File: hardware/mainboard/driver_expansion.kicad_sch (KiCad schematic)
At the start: 17 parts, among them T1 V_{SA}, T10 TestPoint, T11 TestPoint, T12 TestPoint, T13 TestPoint, T14 TestPoint, T15 TestPoint, T2 Gnd, T3 Clk, T4 SClk, T5 Gnd, T6 MOSI, T7 MISO, T8 V_{CC}IO, T9 TestPoint

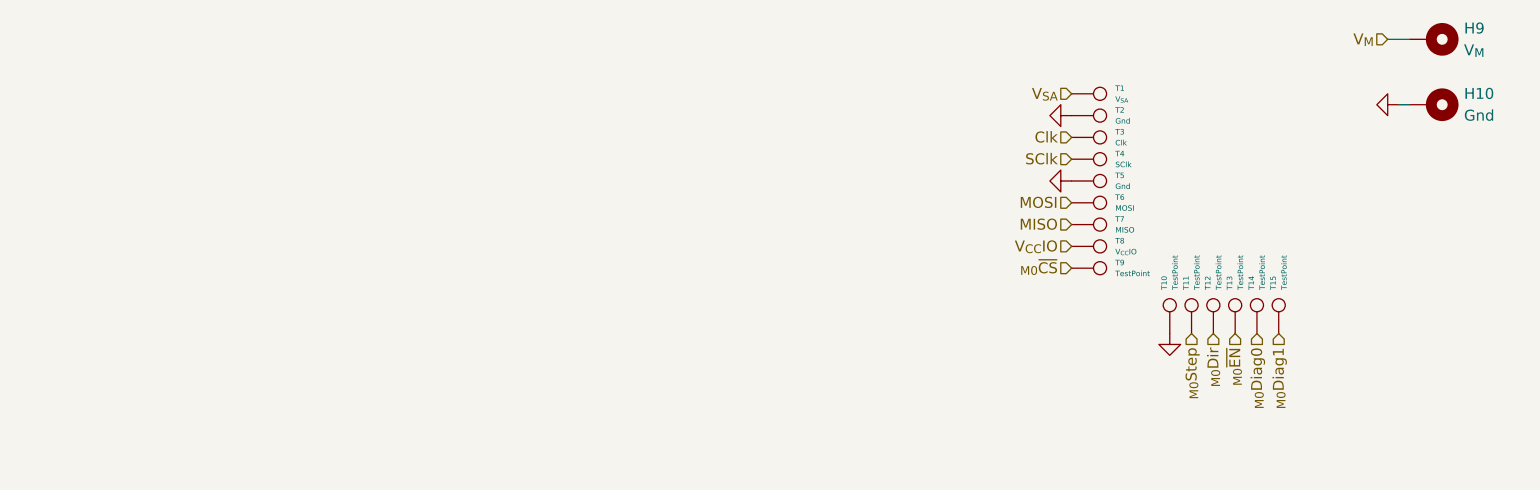
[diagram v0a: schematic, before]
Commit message: added fan / heater ports to mainboard, and footprints for switches, transistors, etc.
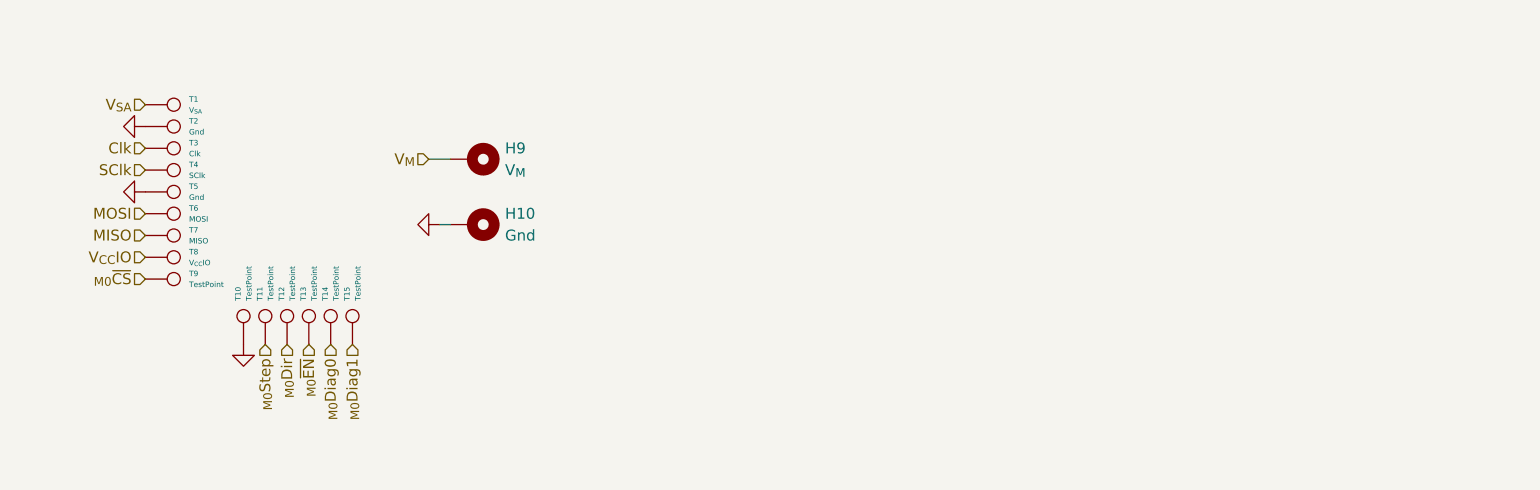
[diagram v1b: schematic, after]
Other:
- title: (none) -> Motor Expansion Socket
- moved on the sheet: H10, H9, T1, T10, T11, T12, T13, T14, T15, T2, T3, T4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

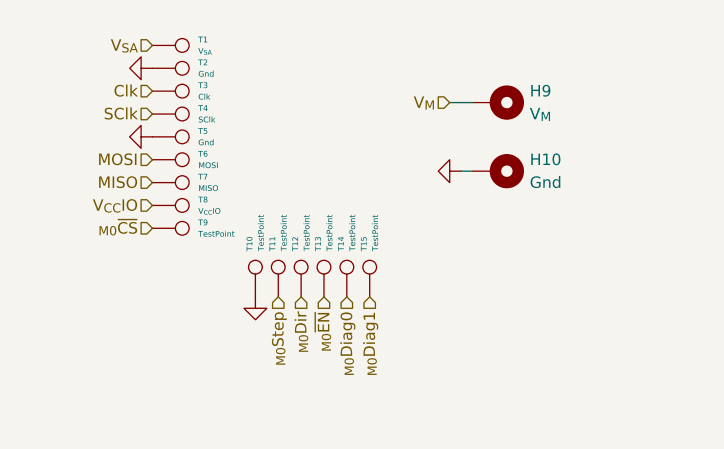
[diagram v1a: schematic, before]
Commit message: saving mainboard, gonna tear out the entire thing and redo in 4-layer
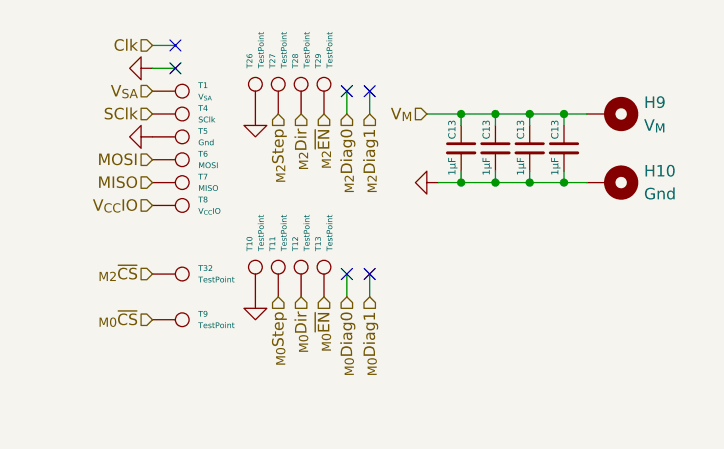
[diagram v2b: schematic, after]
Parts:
- removed T14, T15: TestPoint, corevus:LGA_Spring, symbol Connector:TestPoint
- removed T2: Gnd, corevus:LGA_Spring, symbol Connector:TestPoint
- removed T3: Clk, corevus:LGA_Spring, symbol Connector:TestPoint
- added C13 (x4): 1μF, Capacitor_SMD:C_0805_2012Metric, symbol Device:C_Small
- added T26, T27, T28, T29, T32: TestPoint, corevus:LGA_Spring, symbol Connector:TestPoint
- H10, H9: footprint corevus:M3_PCB_Nut -> corevus:M3_M2.5_PCB_Nut
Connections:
- net GND: now also C13.2, C13.2, C13.2, C13.2, T26.1
- net V_{M}: now also C13.1, C13.1, C13.1, C13.1
- new net _{M2}Dir: T28.1
- new net _{M2}Step: T27.1
- new net _{M2}~{CS}: T32.1
- new net _{M2}~{EN}: T29.1
- no-connect marks 0 -> 6
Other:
- moved on the sheet: H10, H9, T1, T9

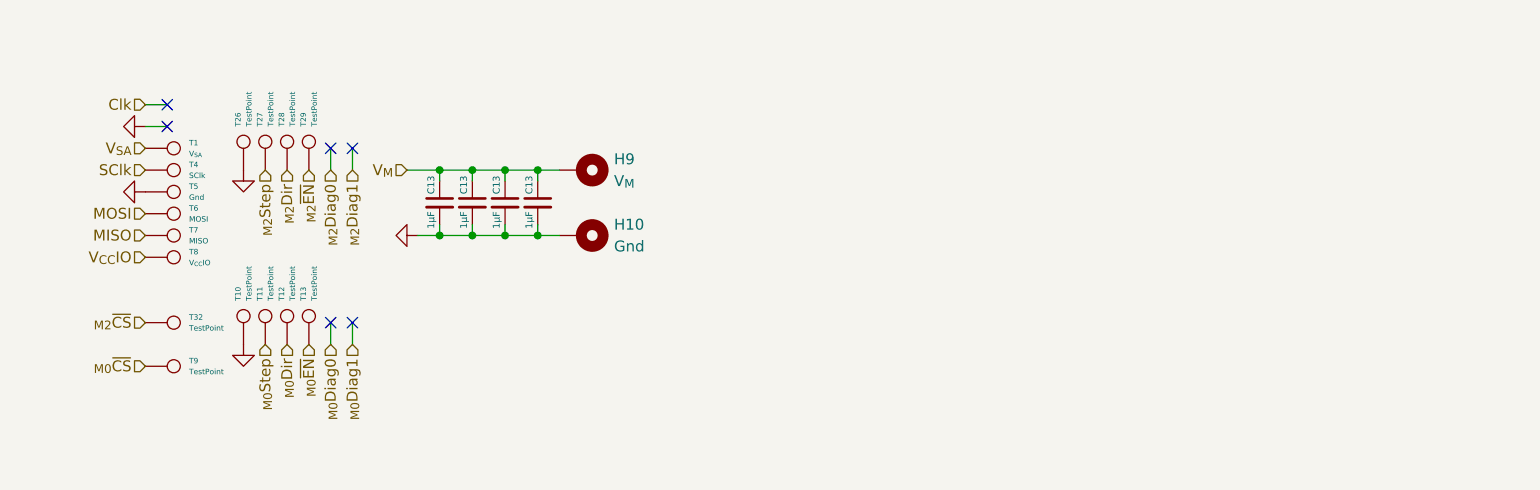
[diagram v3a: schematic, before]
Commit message: redid mainboard, added probe wiring, replacing ncp chip with LM5160 for now
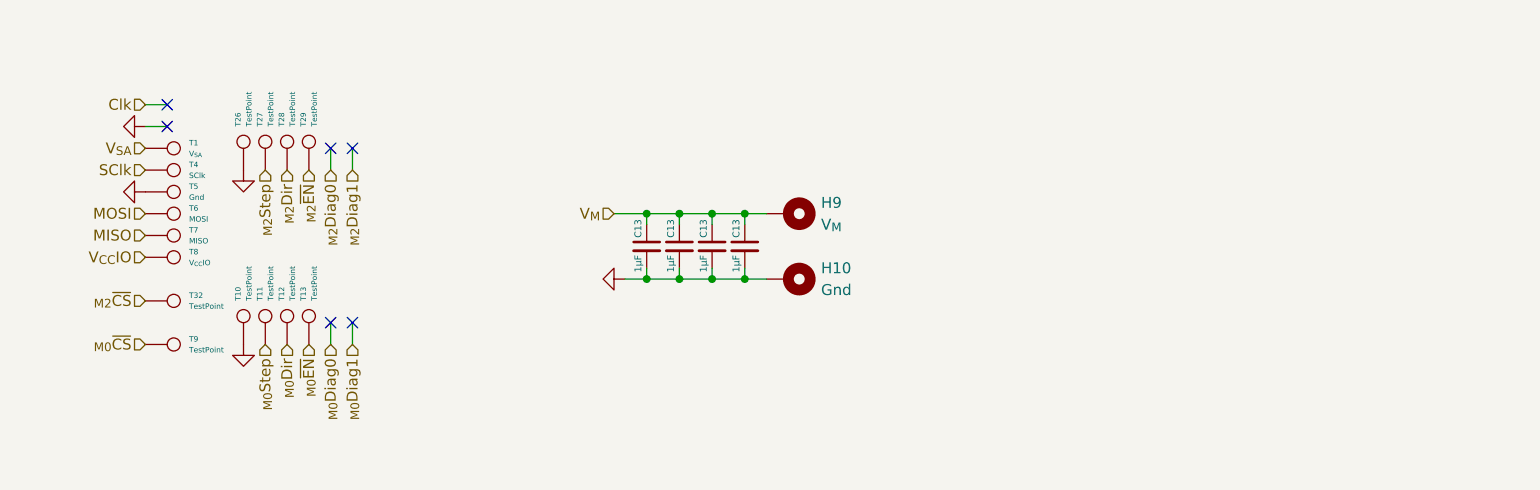
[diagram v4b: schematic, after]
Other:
- moved on the sheet: C13, H10, H9, T32, T9

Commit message: nearing first prototype woot! copyediting over entire board, fixed some mistakes
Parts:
- C13: value 1μF -> 1μF 63V; footprint Capacitor_SMD:C_0805_2012Metric -> Capacitor_SMD:C_1206_3216Metric
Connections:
- net _{M0}~{EN} renamed _{M0}~{En}
- net _{M2}~{EN} renamed _{M2}~{En}
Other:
- moved on the sheet: H10
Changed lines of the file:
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@@
   (junction (at 114.3 66.04) (diameter 0) (color 0 0 0 0)
   )
-  (junction (at 114.3 73.66) (diameter 0) (color 0 0 0 0)
-  )
-  (junction (at 118.11 73.66) (diameter 0) (color 0 0 0 0)
+  (junction (at 114.3 76.2) (diameter 0) (color 0 0 0 0)
+  )
+  (junction (at 118.11 76.2) (diameter 0) (color 0 0 0 0)
   )
   (junction (at 106.68 66.04) (diameter 0) (color 0 0 0 0)
@@
   (junction (at 110.49 66.04) (diameter 0) (color 0 0 0 0)
   )
-  (junction (at 106.68 73.66) (diameter 0) (color 0 0 0 0)
+  (junction (at 106.68 76.2) (diameter 0) (color 0 0 0 0)
   )
   (junction (at 118.11 66.04) (diameter 0) (color 0 0 0 0)
   )
-  (junction (at 110.49 73.66) (diameter 0) (color 0 0 0 0)
+  (junction (at 110.49 76.2) (diameter 0) (color 0 0 0 0)
   )
   (no_connect (at 72.39 58.42))
@@
     (stroke (width 0) (type default))
   )
-  (wire (pts (xy 118.11 73.66) (xy 120.65 73.66))
+  (wire (pts (xy 118.11 76.2) (xy 120.65 76.2))
     (stroke (width 0) (type default))
   )
@@
     (stroke (width 0) (type default))
   )
-  (wire (pts (xy 104.14 73.66) (xy 106.68 73.66))
-    (stroke (width 0) (type default))
-  )
-  (wire (pts (xy 114.3 72.39) (xy 114.3 73.66))
+  (wire (pts (xy 104.14 76.2) (xy 106.68 76.2))
     (stroke (width 0) (type default))
   )
@@
     (stroke (width 0) (type default))
   )
-  (wire (pts (xy 110.49 73.66) (xy 114.3 73.66))
-    (stroke (width 0) (type default))
-  )
-  (wire (pts (xy 106.68 73.66) (xy 110.49 73.66))
-    (stroke (width 0) (type default))
-  )
-  (wire (pts (xy 106.68 72.39) (xy 106.68 73.66))
+  (wire (pts (xy 110.49 76.2) (xy 114.3 76.2))
+    (stroke (width 0) (type default))
+  )
+  (wire (pts (xy 106.68 72.39) (xy 106.68 76.2))
+    (stroke (width 0) (type default))
+  )
+  (wire (pts (xy 106.68 76.2) (xy 110.49 76.2))
     (stroke (width 0) (type default))
   )
@@
     (stroke (width 0) (type default))
   )
-  (wire (pts (xy 114.3 73.66) (xy 118.11 73.66))
+  (wire (pts (xy 114.3 72.39) (xy 114.3 76.2))
+    (stroke (width 0) (type default))
+  )
+  (wire (pts (xy 114.3 76.2) (xy 118.11 76.2))
     (stroke (width 0) (type default))
   )
@@
     (stroke (width 0) (type default))
   )
-  (wire (pts (xy 110.49 72.39) (xy 110.49 73.66))
+  (wire (pts (xy 110.49 72.39) (xy 110.49 76.2))
     (stroke (width 0) (type default))
   )
@@
     (stroke (width 0) (type default))
   )
-  (wire (pts (xy 118.11 72.39) (xy 118.11 73.66))
+  (wire (pts (xy 118.11 72.39) (xy 118.11 76.2))
     (stroke (width 0) (type default))
   )
@@
     (effects (font (size 1.27 1.27)) (justify right))
   )
-  (hierarchical_label "_{M0}~{EN}" (shape input) (at 67.31 81.28 270) (fields_autoplaced)
+  (hierarchical_label "_{M0}~{En}" (shape input) (at 67.31 81.28 270) (fields_autoplaced)
     (effects (font (size 1.27 1.27)) (justify right))
   )
@@
     (effects (font (size 1.27 1.27)) (justify right))
   )
-  (hierarchical_label "_{M2}~{EN}" (shape input) (at 67.31 60.96 270) (fields_autoplaced)
+  (hierarchical_label "_{M2}~{En}" (shape input) (at 67.31 60.96 270) (fields_autoplaced)
     (effects (font (size 1.27 1.27)) (justify right))
   )
@@
       (effects (font (size 0.8 0.8)) (justify left))
     )
-    (property "Value" "1μF" (at 109.49 70.85 90)
+    (property "Value" "1μF 63V" (at 109.49 70.85 90)
       (effects (font (size 0.8 0.8)) (justify right))
     )
-    (property "Footprint" "Capacitor_SMD:C_0805_2012Metric" (at 110.49 69.85 0)
+    (property "Footprint" "Capacitor_SMD:C_1206_3216Metric" (at 110.49 69.85 0)
       (effects (font (size 1.27 1.27)) hide)
     )
@@
       (effects (font (size 0.8 0.8)) (justify left))
     )
-    (property "Value" "1μF" (at 113.3 70.85 90)
+    (property "Value" "1μF 63V" (at 113.3 70.85 90)
       (effects (font (size 0.8 0.8)) (justify right))
     )
-    (property "Footprint" "Capacitor_SMD:C_0805_2012Metric" (at 114.3 69.85 0)
+    (property "Footprint" "Capacitor_SMD:C_1206_3216Metric" (at 114.3 69.85 0)
       (effects (font (size 1.27 1.27)) hide)
     )
@@
       (effects (font (size 0.8 0.8)) (justify left))
     )
-    (property "Value" "1μF" (at 105.68 70.85 90)
+    (property "Value" "1μF 63V" (at 105.68 70.85 90)
       (effects (font (size 0.8 0.8)) (justify right))
     )
-    (property "Footprint" "Capacitor_SMD:C_0805_2012Metric" (at 106.68 69.85 0)
+    (property "Footprint" "Capacitor_SMD:C_1206_3216Metric" (at 106.68 69.85 0)
       (effects (font (size 1.27 1.27)) hide)
     )
@@
     )
   )
-  (symbol (lib_id "Mechanical:MountingHole_Pad") (at 123.19 73.66 270) (unit 1)
-    (in_bom yes) (on_board yes) (dnp no)
-    (property "Reference" "H10" (at 127 72.39 90)
+  (symbol (lib_id "Mechanical:MountingHole_Pad") (at 123.19 76.2 270) (unit 1)
+    (in_bom yes) (on_board yes) (dnp no)
+    (property "Reference" "H10" (at 127 74.93 90)
       (effects (font (size 1.27 1.27)) (justify left))
     )
-    (property "Value" "Gnd" (at 127 74.93 90)
+    (property "Value" "Gnd" (at 127 77.47 90)
       (effects (font (size 1.27 1.27)) (justify left))
     )
-    (property "Footprint" "corevus:M3_M2.5_PCB_Nut" (at 123.19 73.66 0)
-      (effects (font (size 1.27 1.27)) hide)
-    )
-    (property "Datasheet" "~" (at 123.19 73.66 0)
+    (property "Footprint" "corevus:M3_M2.5_PCB_Nut" (at 123.19 76.2 0)
+      (effects (font (size 1.27 1.27)) hide)
+    )
+    (property "Datasheet" "~" (at 123.19 76.2 0)
       (effects (font (size 1.27 1.27)) hide)
     )
@@
     )
   )
-  (symbol (lib_id "power:GND") (at 104.14 73.66 270) (unit 1)
-    (in_bom yes) (on_board yes) (dnp no)
-    (property "Reference" "#PWR?" (at 97.79 73.66 0)
-      (effects (font (size 1.27 1.27)) hide)
-    )
-    (property "Value" "GND" (at 101.6 73.66 90)
+  (symbol (lib_id "power:GND") (at 104.14 76.2 270) (unit 1)
+    (in_bom yes) (on_board yes) (dnp no)
+    (property "Reference" "#PWR?" (at 97.79 76.2 0)
+      (effects (font (size 1.27 1.27)) hide)
+    )
+    (property "Value" "GND" (at 101.6 76.2 90)
       (effects (font (size 1.27 1.27)) (justify right) hide)
     )
-    (property "Footprint" "" (at 104.14 73.66 0)
-      (effects (font (size 1.27 1.27)) hide)
-    )
-    (property "Datasheet" "" (at 104.14 73.66 0)
+    (property "Footprint" "" (at 104.14 76.2 0)
+      (effects (font (size 1.27 1.27)) hide)
+    )
+    (property "Datasheet" "" (at 104.14 76.2 0)
       (effects (font (size 1.27 1.27)) hide)
     )
@@
       (effects (font (size 0.8 0.8)) (justify left))
     )
-    (property "Value" "1μF" (at 117.11 70.85 90)
+    (property "Value" "1μF 63V" (at 117.11 70.85 90)
       (effects (font (size 0.8 0.8)) (justify right))
     )
-    (property "Footprint" "Capacitor_SMD:C_0805_2012Metric" (at 118.11 69.85 0)
-      (effects (font (size 1.27 1.27)) hide)
-    )
+    (property "Footprint" "Capacitor_SMD:C_1206_3216Metric" (at 118.11 69.85 0)
+      (effects (font (size 1.27 1.27)) hide)
+    )

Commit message: redoing board for version alpha 0.2
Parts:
- renumbered H9 to H5, H10 to H6, T27 to T11, T11 to T12, T28 to T13, T12 to T14, T29 to T15, T13 to T16, T4 to T2, T5 to T3, T6 to T4, T7 to T5, T8 to T6, T32 to T7, T9 to T8, T26 to T9
